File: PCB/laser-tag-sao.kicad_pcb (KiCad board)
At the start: 2 copper layers, 16 parts, among them J1 SAO Connector, Q1 PN2222A, SW1 SW_Push, SW2 SW_Push, SW3 SW_Push, U1 ATTINY84A-PU, U2 TSOP38438, U3 OLED_0.91_128x32

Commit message: laying out components on my board
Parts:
- J1, JP1, JP2: moved to B.Cu
- R1, R2, R4: footprint Resistor_THT:R_Axial_DIN0309_L9.0mm_D3.2mm_P12.70mm_Horizontal -> Resistor_THT:R_Axial_DIN0204_L3.6mm_D1.6mm_P5.08mm_Horizontal
- moved JP1 96.4 mm to (200.2, 71.0), turned to -90 degrees
- moved JP2 94.7 mm to (197.5, 71.0), turned to 90 degrees
- moved BZ1 87.8 mm to (220.6, 74.0)
- moved SW2 80.7 mm to (199.5, 79.8)
- moved U3 74.8 mm to (180.0, 37.0), turned to -90 degrees
- moved C1 74.0 mm to (181.5, 72.5), turned to 90 degrees
- moved U1 65.4 mm to (184.9, 74.8), turned to 90 degrees
- moved SW1 61.6 mm to (177.0, 79.8)
- moved J1 59.8 mm to (190.2, 79.0), turned to -90 degrees
- moved R4 59.3 mm to (187.2, 82.3), turned to 90 degrees
- moved R1 40.4 mm to (166.5, 74.0), turned to 180 degrees
- moved R2 34.8 mm to (161.5, 76.5)
- moved Q1 34.8 mm to (162.7, 70.5)
- moved U2 29.0 mm to (156.8, 82.5), turned to 90 degrees
- moved D1 17.3 mm to (155.7, 71.5)
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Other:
- board outline added: 99.8 x 43.6 mm

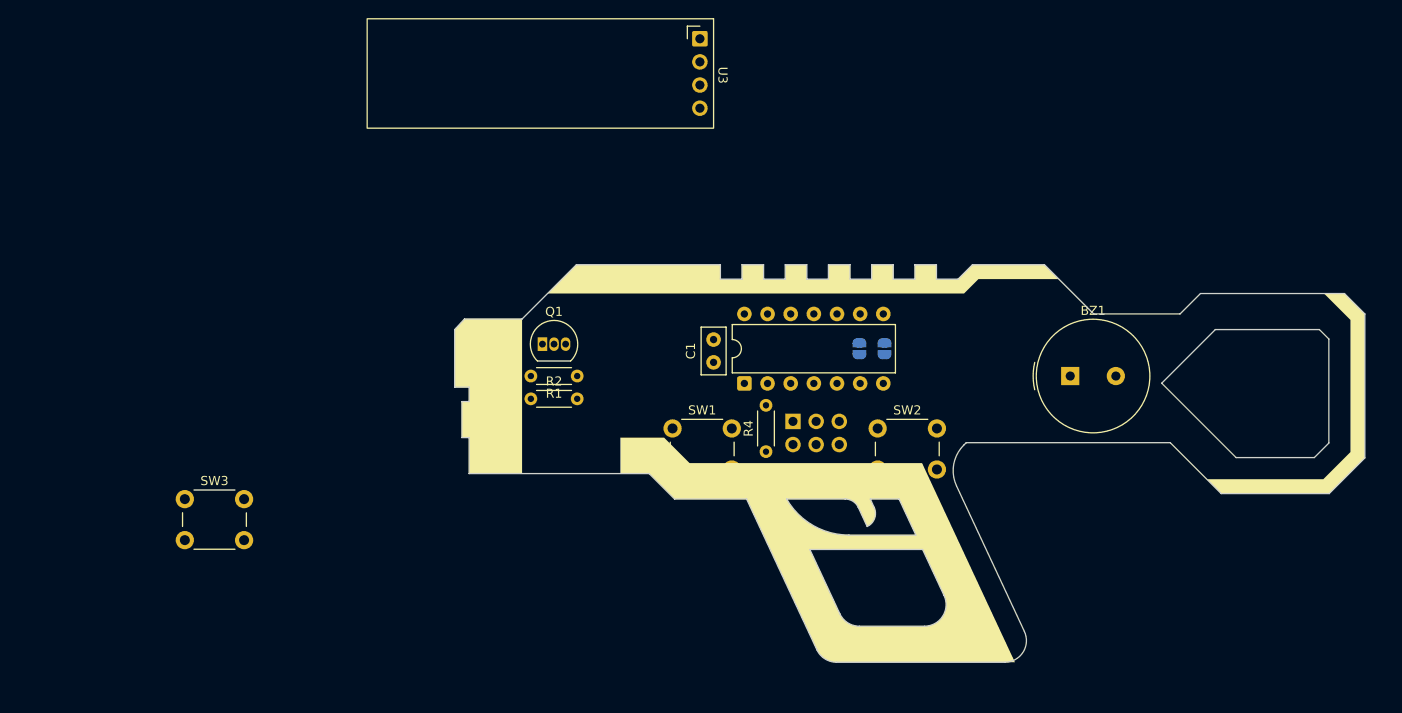
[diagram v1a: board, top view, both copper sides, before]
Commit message: adding neopixels and soldermask openings
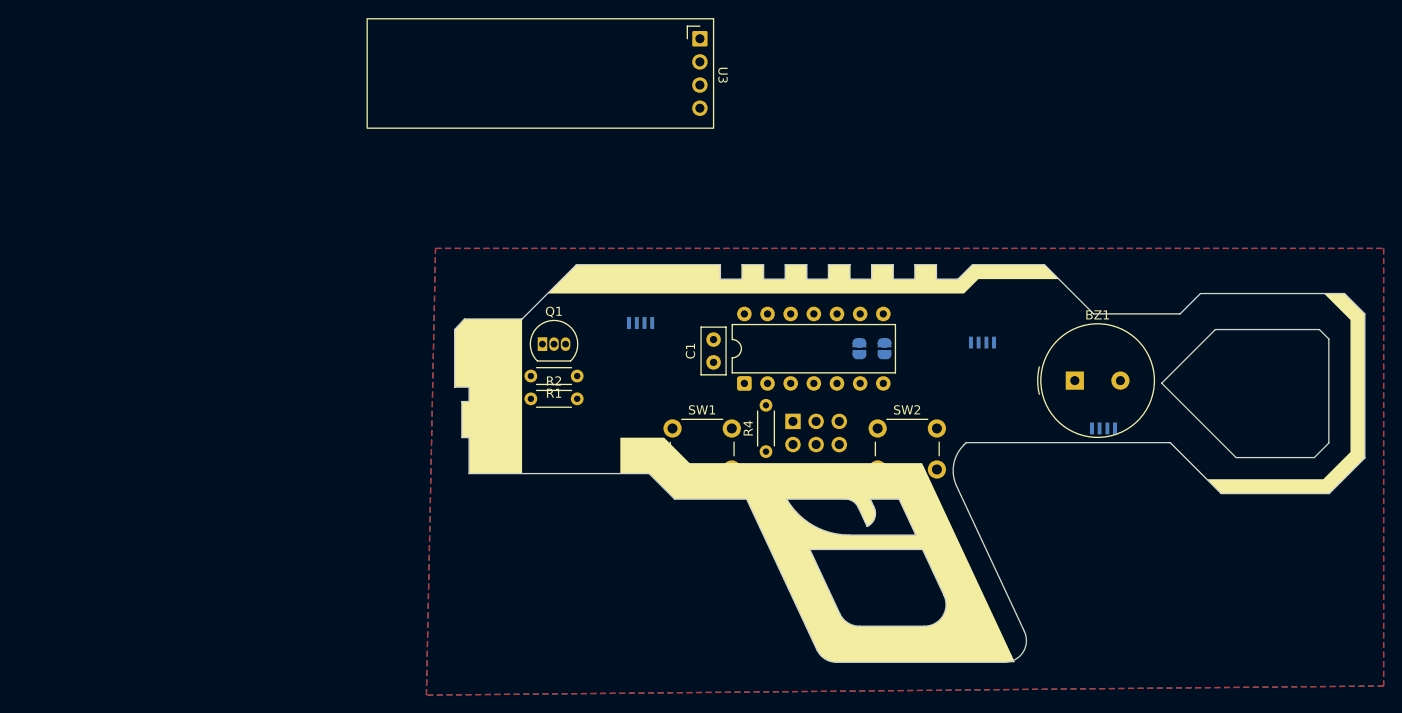
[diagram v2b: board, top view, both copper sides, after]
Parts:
- removed SW3: SW_Push, Button_Switch_THT:SW_PUSH_6mm
- added D2: WS2812B-4020, kai's library:LED_WS2812B-4020, B.Cu at (224.3, 78.9)
- added D3: WS2812B-4020, kai's library:LED_WS2812B-4020, B.Cu at (173.5, 69.0)
- added D4: WS2812B-4020, kai's library:LED_WS2812B-4020, B.Cu at (211.0, 71.2)
- moved U2 4.87 mm to (158.5, 78.0), turned to -90 degrees
- moved BZ1 0.71 mm to (221.1, 74.5)
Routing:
- added copper zone on B.Cu, net GND
- added copper zone on F.Cu, net GND

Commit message: finished routing the board, 0 DRC errors
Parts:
- moved D2 51.7 mm to (173.5, 69.0), turned to 0 degrees
- moved U3 38.7 mm to (177.4, 75.6), turned to 90 degrees
- moved D3 38.0 mm to (210.8, 76.2), turned to 180 degrees
- moved D4 15.3 mm to (224.2, 78.9), turned to 180 degrees
- moved Q1 2.59 mm to (165.3, 70.0), turned to 180 degrees
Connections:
- U1 pad 10: /PUSH2 -> unconnected-(U1-PA3-Pad10)
- U1 pad 3: /PUSH3 -> /PUSH2
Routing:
- net +3V3: track 0.00 -> 95.8 mm, vias 0 -> 2
- net /MISO/IR_TX: track 0.00 -> 63.7 mm, vias 0 -> 2
- net Net-(D2-DOUT): track 0.00 -> 48.7 mm, vias 0 -> 2
- net /BUZZER: track 0.00 -> 43.1 mm
- net /IR_RX: track 0.00 -> 38.2 mm
- net /LED: track 0.00 -> 32.1 mm, vias 0 -> 2
- net /SCK/SCL: track 0.00 -> 28.0 mm
- net /PUSH2: track 0.00 -> 27.7 mm
- net /PUSH1: track 0.00 -> 23.9 mm
- net Net-(J1-Pin_6): track 0.00 -> 22.3 mm, vias 0 -> 1
- net /OLED_SCL: track 0.00 -> 14.0 mm
- net /RESET: track 0.00 -> 13.1 mm
- net Net-(D3-DOUT): track 0.00 -> 13.1 mm
- net Net-(J1-Pin_5): track 0.00 -> 12.0 mm, vias 0 -> 1
- net /OLED_SDA: track 0.00 -> 10.6 mm
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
